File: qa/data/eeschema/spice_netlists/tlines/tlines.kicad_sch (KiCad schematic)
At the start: 6 parts, among them T1 TLINE, T2 TLINE

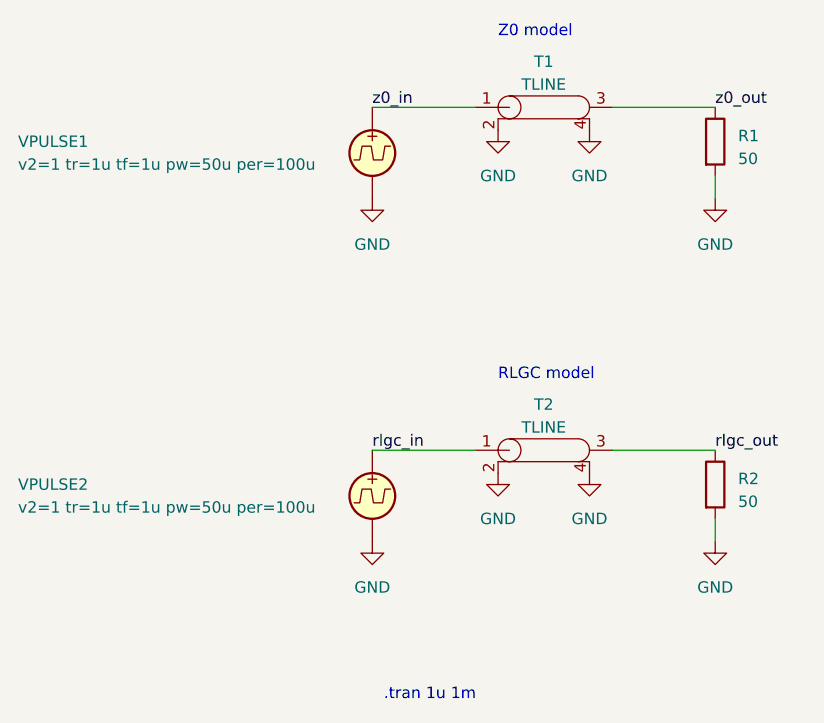
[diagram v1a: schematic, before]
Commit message: Spice Model Editor: Prune superfluous or simple but oddly-specific models and params
Some Spice or Ngspice models are oddly-specific, i.e. they can be easily
realized using primitives and have only narrow applications. E.g. SFFM,
AM (actually single-frequency AM), semiconductor resistor, semiconductor
capacitor, semicondutor inductor.

Some parameters are superfluous; in primitive models like sources or
transmission lines these should removed in favor of more direct ones,
e.g. phase offset should be replaced with time offset where possible.
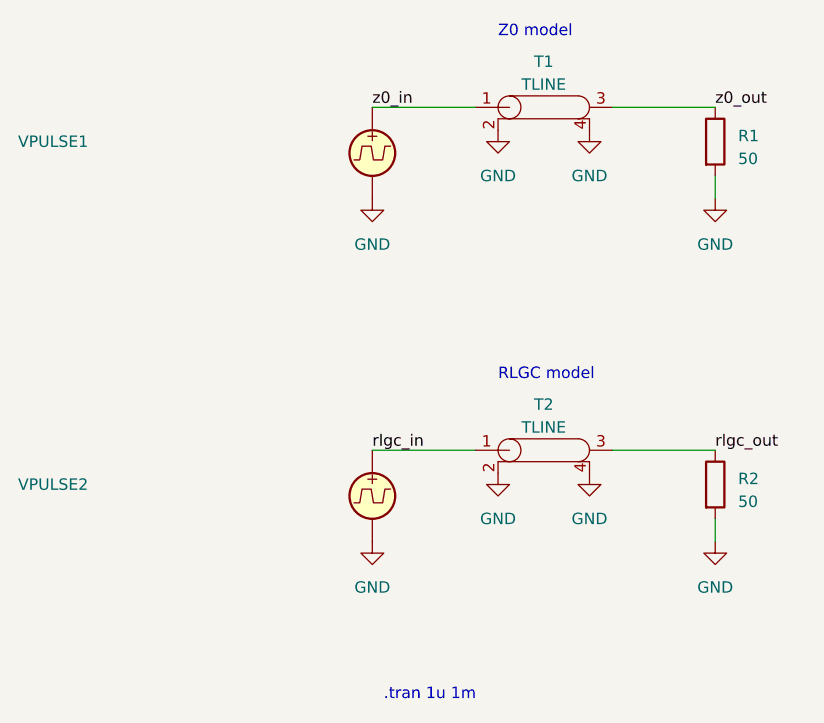
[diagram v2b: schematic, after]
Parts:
- VPULSE1, VPULSE2: value v2=1 tr=1u tf=1u pw=50u per=100u -> (none)
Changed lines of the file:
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@@
       (effects (font (size 1.27 1.27)) (justify left))
     )
-    (property "Value" "v2=1 tr=1u tf=1u pw=50u per=100u" (id 1) (at 87.63 82.55 0)
+    (property "Value" "" (id 1) (at 87.63 82.55 0)
       (effects (font (size 1.27 1.27)) (justify left))
     )
@@
       (effects (font (size 1.27 1.27)) (justify left))
     )
-    (property "Value" "v2=1 tr=1u tf=1u pw=50u per=100u" (id 1) (at 87.63 120.65 0)
+    (property "Value" "" (id 1) (at 87.63 120.65 0)
       (effects (font (size 1.27 1.27)) (justify left))
     )
@@
     )
     (path "/56fc236a-df5f-49ef-9b92-3227f86197b4"
-      (reference "VPULSE1") (unit 1) (value "v2=1 tr=1u tf=1u pw=50u per=100u") (footprint "")
+      (reference "VPULSE1") (unit 1) (value "v2=1 tr=1u tf=1u tw=50u per=100u") (footprint "")
     )
     (path "/fcc0dfa9-c624-4a32-a3d3-4c36ee7b0fe6"
-      (reference "VPULSE2") (unit 1) (value "v2=1 tr=1u tf=1u pw=50u per=100u") (footprint "")
-    )
-  )
+      (reference "VPULSE2") (unit 1) (value "v2=1 tr=1u tf=1u tw=50u per=100u") (footprint "")
+    )
+  )

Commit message: Infer tline model from Reference and Value
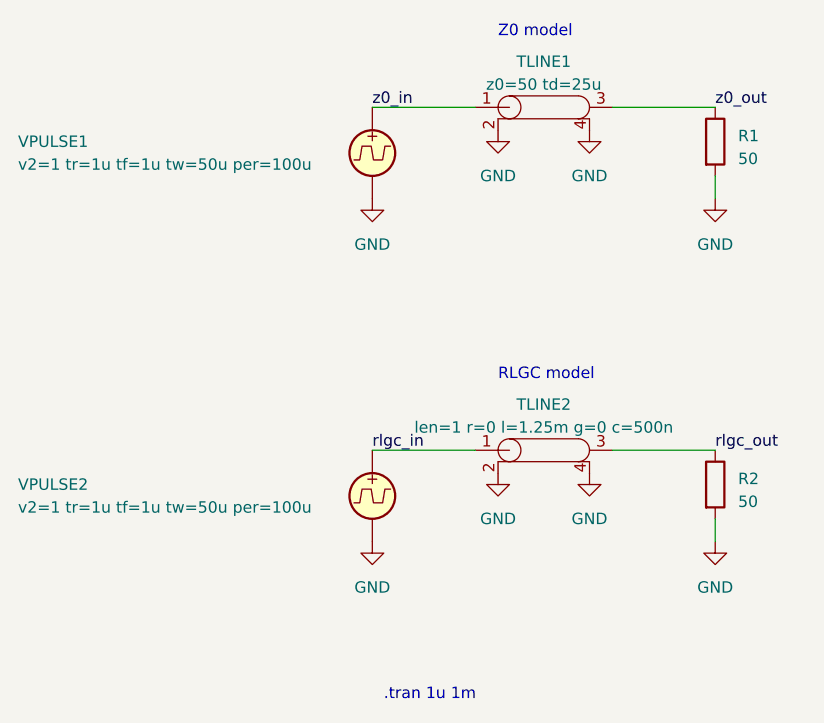
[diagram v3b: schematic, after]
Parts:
- TLINE1: renamed from T1; value TLINE -> z0=50 td=25u; Model_Device TLINE -> (none); Model_Params z0=50 td=25u -> (none); Model_Pins 1 2 3 4 -> (none); Model_Type Z0 -> (none)
- TLINE2: renamed from T2; value TLINE -> len=1 r=0 l=1.25m g=0 c=500n; Model_Device TLINE -> (none); Model_Params len=1 r=0 l=1.25m g=0 c=500n -> (none); Model_Pins 1 2 3 4 -> (none); Model_Type RLGC -> (none)
- VPULSE1, VPULSE2: value (none) -> v2=1 tr=1u tf=1u tw=50u per=100u
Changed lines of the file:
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@@
+    (stroke (width 0) (type default))
+  )
+  (wire (pts (xy 153.67 76.2) (xy 165.1 76.2))
     (stroke (width 0) (type default))
   )
@@
   )
   (wire (pts (xy 127 76.2) (xy 138.43 76.2))
-    (stroke (width 0) (type default))
-  )
-  (wire (pts (xy 153.67 76.2) (xy 165.1 76.2))
     (stroke (width 0) (type default))
   )
@@
   (symbol (lib_id "Transmission_Line:TLINE") (at 146.05 114.3 0) (unit 1)
     (in_bom no) (on_board no) (fields_autoplaced)
-    (property "Reference" "T2" (id 0) (at 146.0509 109.22 0)
-      (effects (font (size 1.27 1.27)))
-    )
-    (property "Value" "TLINE" (id 1) (at 146.0509 111.76 0)
+    (property "Reference" "TLINE2" (id 0) (at 146.0509 109.22 0)
+      (effects (font (size 1.27 1.27)))
+    )
+    (property "Value" "len=1 r=0 l=1.25m g=0 c=500n" (id 1) (at 146.0509 111.76 0)
       (effects (font (size 1.27 1.27)))
     )
@@
     )
     (property "Datasheet" "http://ngspice.sourceforge.net/docs/ngspice-36-manual.pdf#7f" (id 3) (at 146.05 109.22 0)
-      (effects (font (size 1.27 1.27)) hide)
-    )
-    (property "Model_Device" "TLINE" (id 4) (at 146.05 114.3 0)
-      (effects (font (size 1.27 1.27)) hide)
-    )
-    (property "Model_Type" "RLGC" (id 5) (at 146.05 114.3 0)
-      (effects (font (size 1.27 1.27)) hide)
-    )
-    (property "Model_Pins" "1 2 3 4" (id 6) (at 146.05 114.3 0)
-      (effects (font (size 1.27 1.27)) hide)
-    )
-    (property "Model_Params" "len=1 r=0 l=1.25m g=0 c=500n" (id 7) (at 146.05 114.3 0)
       (effects (font (size 1.27 1.27)) hide)
     )
@@
       (effects (font (size 1.27 1.27)) (justify left))
     )
-    (property "Value" "" (id 1) (at 87.63 82.55 0)
+    (property "Value" "v2=1 tr=1u tf=1u tw=50u per=100u" (id 1) (at 87.63 82.55 0)
       (effects (font (size 1.27 1.27)) (justify left))
     )
@@
   (symbol (lib_id "Transmission_Line:TLINE") (at 146.05 76.2 0) (unit 1)
     (in_bom no) (on_board no) (fields_autoplaced)
-    (property "Reference" "T1" (id 0) (at 146.0509 71.12 0)
-      (effects (font (size 1.27 1.27)))
-    )
-    (property "Value" "TLINE" (id 1) (at 146.0509 73.66 0)
+    (property "Reference" "TLINE1" (id 0) (at 146.0509 71.12 0)
+      (effects (font (size 1.27 1.27)))
+    )
+    (property "Value" "z0=50 td=25u" (id 1) (at 146.0509 73.66 0)
       (effects (font (size 1.27 1.27)))
     )
@@
     )
     (property "Datasheet" "http://ngspice.sourceforge.net/docs/ngspice-36-manual.pdf#7f" (id 3) (at 146.05 71.12 0)
-      (effects (font (size 1.27 1.27)) hide)
-    )
-    (property "Model_Device" "TLINE" (id 4) (at 146.05 76.2 0)
-      (effects (font (size 1.27 1.27)) hide)
-    )
-    (property "Model_Type" "Z0" (id 5) (at 146.05 76.2 0)
-      (effects (font (size 1.27 1.27)) hide)
-    )
-    (property "Model_Pins" "1 2 3 4" (id 6) (at 146.05 76.2 0)
-      (effects (font (size 1.27 1.27)) hide)
-    )
-    (property "Model_Params" "z0=50 td=25u" (id 7) (at 146.05 76.2 0)
       (effects (font (size 1.27 1.27)) hide)
     )
@@
       (effects (font (size 1.27 1.27)) (justify left))
     )
-    (property "Value" "" (id 1) (at 87.63 120.65 0)
+    (property "Value" "v2=1 tr=1u tf=1u tw=50u per=100u" (id 1) (at 87.63 120.65 0)
       (effects (font (size 1.27 1.27)) (justify left))
     )
@@
     )
     (path "/b320600b-eef1-4883-916c-38700f3f43d4"
-      (reference "T1") (unit 1) (value "TLINE") (footprint "")
+      (reference "TLINE1") (unit 1) (value "z0=50 td=25u") (footprint "")
     )
     (path "/34b3fec2-c790-40cf-bb63-dd642fff2299"
-      (reference "T2") (unit 1) (value "TLINE") (footprint "")
+      (reference "TLINE2") (unit 1) (value "len=1 r=0 l=1.25m g=0 c=500n") (footprint "")
     )
     (path "/56fc236a-df5f-49ef-9b92-3227f86197b4"
